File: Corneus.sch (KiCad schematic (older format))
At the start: 146 parts, among them J1 USB_B_Micro, Q1 Q_NPN_BCE, SW1 SW_Push, U1 ATmega32U4-AU, Y1 16MHz

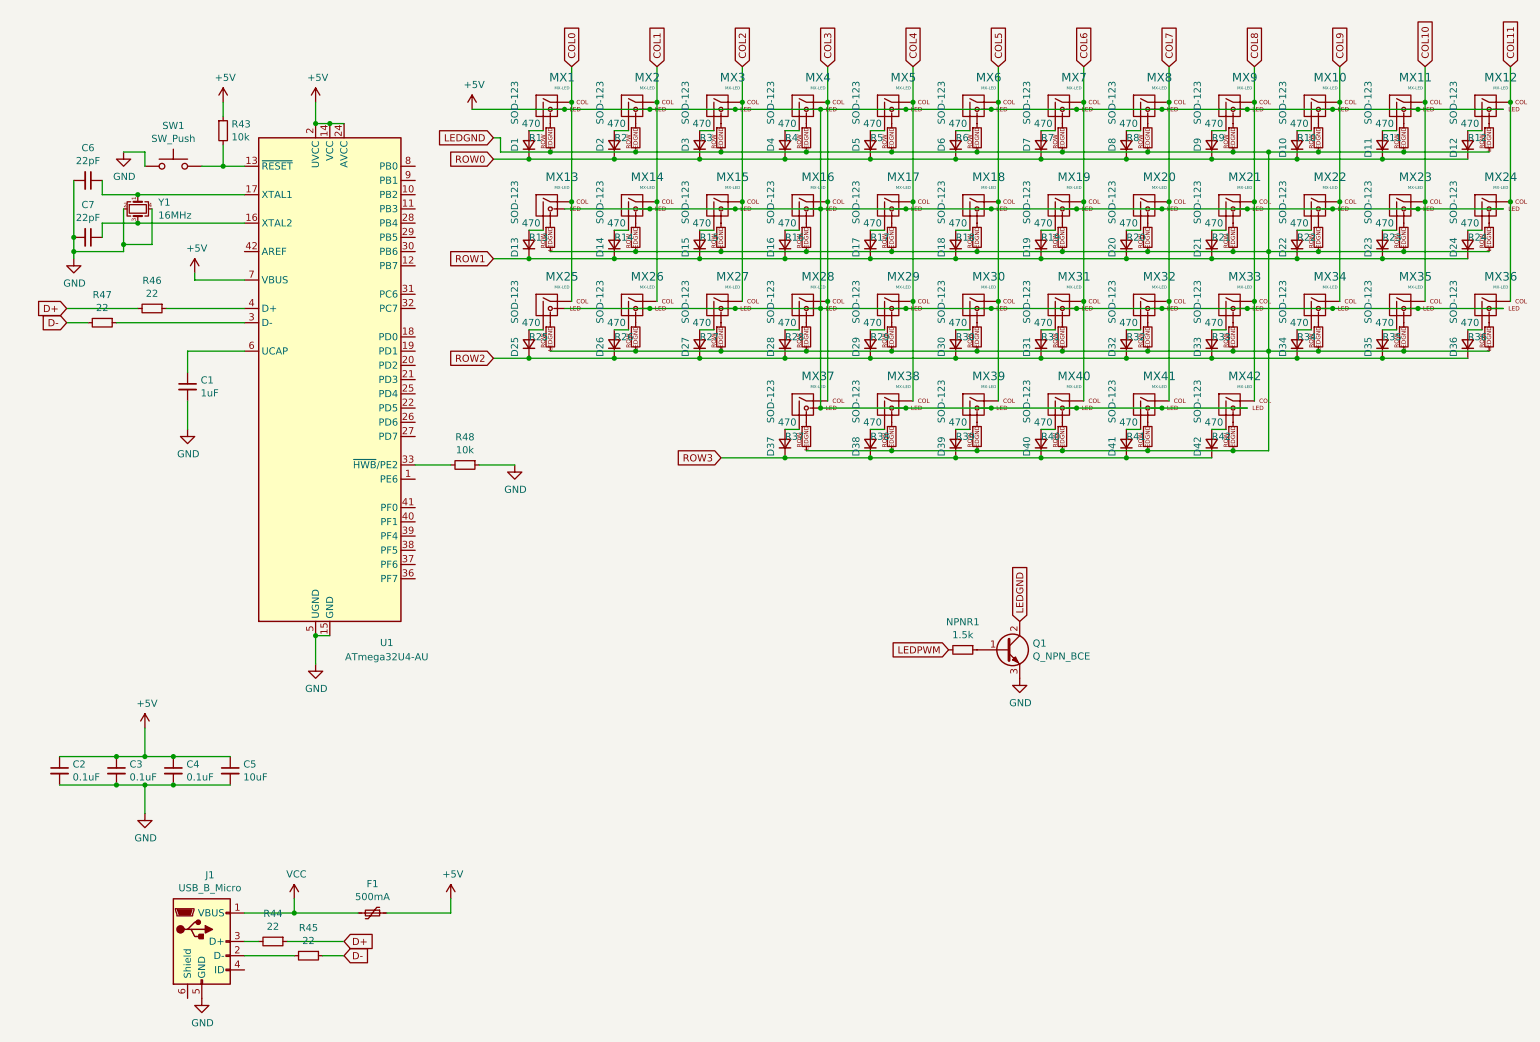
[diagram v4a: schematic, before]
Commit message: added ESD
added ESD IC used in Masterzen's PCB design guide, the CPM43, and the Voyager40
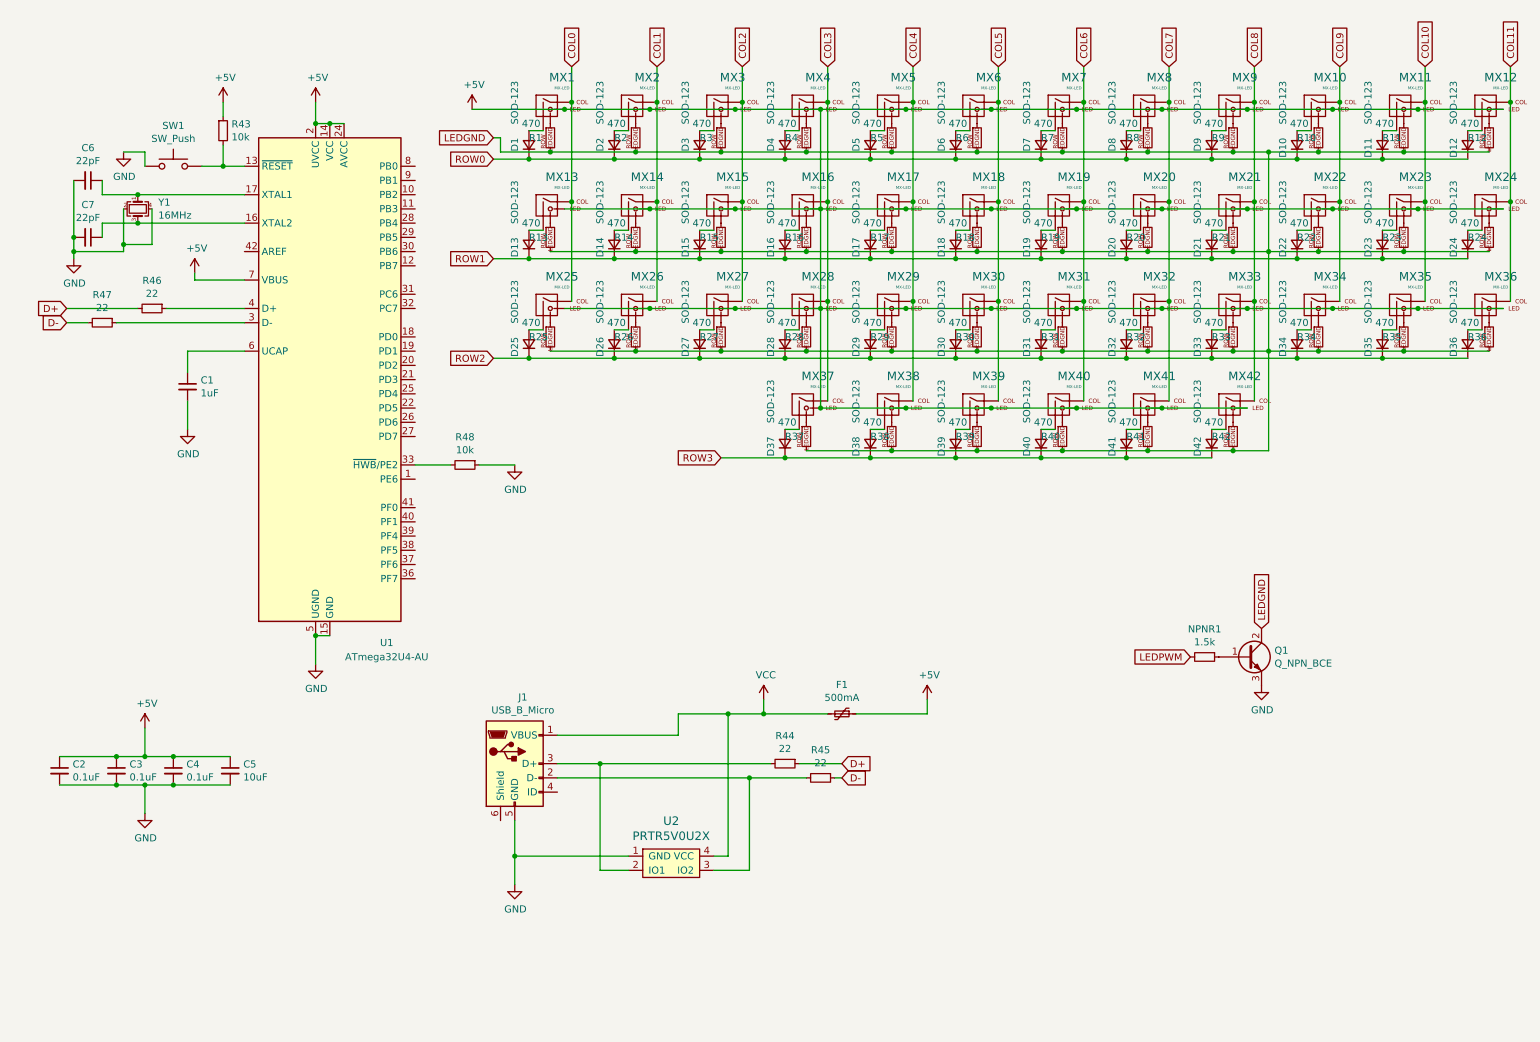
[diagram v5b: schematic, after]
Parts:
- added U2: PRTR5V0U2X, symbol random-keyboard-parts:PRTR5V0U2X
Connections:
- net GND: now also U2.1 (GND)
- net VCC: now also U2.4 (VCC)
- net at J1.2 (D-), R45.2: now also U2.3 (IO2)
- net at J1.3 (D+), R44.2: now also U2.2 (IO1)
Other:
- moved on the sheet: F1, J1, NPNR1, Q1, R44, R45
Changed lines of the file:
@@
 L Connector:USB_B_Micro J1
 U 1 1 5EED7A0C
-P 1800 6950
-F 0 "J1" H 1857 7417 50  0000 C CNN
-F 1 "USB_B_Micro" H 1857 7326 50  0000 C CNN
-F 2 "" H 1950 6900 50  0001 C CNN
-F 3 "~" H 1950 6900 50  0001 C CNN
-	1    1800 6950
+P 4000 5700
+F 0 "J1" H 4057 6167 50  0000 C CNN
+F 1 "USB_B_Micro" H 4057 6076 50  0000 C CNN
+F 2 "" H 4150 5650 50  0001 C CNN
+F 3 "~" H 4150 5650 50  0001 C CNN
+	1    4000 5700
 	1    0    0    -1
 $EndComp
@@
 L Device:Polyfuse_Small F1
 U 1 1 5EED8839
-P 3000 6750
-F 0 "F1" V 2795 6750 50  0000 C CNN
-F 1 "500mA" V 2886 6750 50  0000 C CNN
-F 2 "" H 3050 6550 50  0001 L CNN
-F 3 "~" H 3000 6750 50  0001 C CNN
-	1    3000 6750
+P 6300 5350
+F 0 "F1" V 6095 5350 50  0000 C CNN
+F 1 "500mA" V 6186 5350 50  0000 C CNN
+F 2 "" H 6350 5150 50  0001 L CNN
+F 3 "~" H 6300 5350 50  0001 C CNN
+	1    6300 5350
 	0    1    1    0
 $EndComp
@@
 L power:VCC #PWR?
 U 1 1 5EEDA4E1
-P 2450 6650
-F 0 "#PWR?" H 2450 6500 50  0001 C CNN
-F 1 "VCC" H 2465 6823 50  0000 C CNN
-F 2 "" H 2450 6650 50  0001 C CNN
-F 3 "" H 2450 6650 50  0001 C CNN
-	1    2450 6650
+P 5750 5250
+F 0 "#PWR?" H 5750 5100 50  0001 C CNN
+F 1 "VCC" H 5765 5423 50  0000 C CNN
+F 2 "" H 5750 5250 50  0001 C CNN
+F 3 "" H 5750 5250 50  0001 C CNN
+	1    5750 5250
 	1    0    0    -1
 $EndComp
@@
 L power:+5V #PWR?
 U 1 1 5EEDB21B
-P 3550 6650
-F 0 "#PWR?" H 3550 6500 50  0001 C CNN
-F 1 "+5V" H 3565 6823 50  0000 C CNN
-F 2 "" H 3550 6650 50  0001 C CNN
-F 3 "" H 3550 6650 50  0001 C CNN
-	1    3550 6650
-	1    0    0    -1
-$EndComp
-Wire Wire Line
-	3550 6650 3550 6750
-Wire Wire Line
-	3550 6750 3100 6750
-Wire Wire Line
-	2900 6750 2450 6750
-Wire Wire Line
-	2450 6650 2450 6750
-Connection ~ 2450 6750
-Wire Wire Line
-	2450 6750 2100 6750
-Text GLabel 2800 6950 2    50   Input ~ 0
+P 6900 5250
+F 0 "#PWR?" H 6900 5100 50  0001 C CNN
+F 1 "+5V" H 6915 5423 50  0000 C CNN
+F 2 "" H 6900 5250 50  0001 C CNN
+F 3 "" H 6900 5250 50  0001 C CNN
+	1    6900 5250
+	1    0    0    -1
+$EndComp
+Wire Wire Line
+	6200 5350 5750 5350
+Wire Wire Line
+	5750 5250 5750 5350
+Text GLabel 6300 5700 2    50   Input ~ 0
 D+
-Text GLabel 2800 7050 2    50   Input ~ 0
+Text GLabel 6300 5800 2    50   Input ~ 0
 D-
 $Comp
 L power:GND #PWR?
 U 1 1 5EEDF093
-P 1800 7350
-F 0 "#PWR?" H 1800 7100 50  0001 C CNN
-F 1 "GND" H 1805 7177 50  0000 C CNN
-F 2 "" H 1800 7350 50  0001 C CNN
-F 3 "" H 1800 7350 50  0001 C CNN
-	1    1800 7350
+P 4000 6550
+F 0 "#PWR?" H 4000 6300 50  0001 C CNN
+F 1 "GND" H 4005 6377 50  0000 C CNN
+F 2 "" H 4000 6550 50  0001 C CNN
+F 3 "" H 4000 6550 50  0001 C CNN
+	1    4000 6550
 	1    0    0    -1
 $EndComp
@@
 L Device:Q_NPN_BCE Q1
 U 1 1 5F5CD88C
-P 7450 4900
-F 0 "Q1" H 7641 4946 50  0000 L CNN
-F 1 "Q_NPN_BCE" H 7641 4855 50  0000 L CNN
-F 2 "" H 7650 5000 50  0001 C CNN
-F 3 "~" H 7450 4900 50  0001 C CNN
-	1    7450 4900
+P 9150 4950
+F 0 "Q1" H 9341 4996 50  0000 L CNN
+F 1 "Q_NPN_BCE" H 9341 4905 50  0000 L CNN
+F 2 "" H 9350 5050 50  0001 C CNN
+F 3 "~" H 9150 4950 50  0001 C CNN
+	1    9150 4950
 	1    0    0    -1
 $EndComp
@@
 L Device:R_Small NPNR1
 U 1 1 5F5CF76A
-P 7150 4900
-F 0 "NPNR1" V 6954 4900 50  0000 C CNN
-F 1 "1.5k" V 7045 4900 50  0000 C CNN
-F 2 "" H 7150 4900 50  0001 C CNN
-F 3 "~" H 7150 4900 50  0001 C CNN
-	1    7150 4900
+P 8850 4950
+F 0 "NPNR1" V 8654 4950 50  0000 C CNN
+F 1 "1.5k" V 8745 4950 50  0000 C CNN
+F 2 "" H 8850 4950 50  0001 C CNN
+F 3 "~" H 8850 4950 50  0001 C CNN
+	1    8850 4950
 	0    1    1    0
 $EndComp
-Text GLabel 7050 4900 0    50   Input ~ 0
+Text GLabel 8750 4950 0    50   Input ~ 0
 LEDPWM
 $Comp
 L power:GND #PWR?
 U 1 1 5F5D128A
-P 7550 5100
-F 0 "#PWR?" H 7550 4850 50  0001 C CNN
-F 1 "GND" H 7555 4927 50  0000 C CNN
-F 2 "" H 7550 5100 50  0001 C CNN
-F 3 "" H 7550 5100 50  0001 C CNN
-	1    7550 5100
-	1    0    0    -1
-$EndComp
-Text GLabel 7550 4700 1    50   Input ~ 0
+P 9250 5150
+F 0 "#PWR?" H 9250 4900 50  0001 C CNN
+F 1 "GND" H 9255 4977 50  0000 C CNN
+F 2 "" H 9250 5150 50  0001 C CNN
+F 3 "" H 9250 5150 50  0001 C CNN
+	1    9250 5150
+	1    0    0    -1
+$EndComp
+Text GLabel 9250 4750 1    50   Input ~ 0
 LEDGND
 $Comp
 L Device:R_Small R44
 U 1 1 5F5EB1F7
-P 2300 6950
-F 0 "R44" V 2104 6950 50  0000 C CNN
-F 1 "22" V 2195 6950 50  0000 C CNN
-F 2 "" H 2300 6950 50  0001 C CNN
-F 3 "~" H 2300 6950 50  0001 C CNN
-	1    2300 6950
+P 5900 5700
+F 0 "R44" V 5704 5700 50  0000 C CNN
+F 1 "22" V 5795 5700 50  0000 C CNN
+F 2 "" H 5900 5700 50  0001 C CNN
+F 3 "~" H 5900 5700 50  0001 C CNN
+	1    5900 5700
 	0    1    1    0
 $EndComp
@@
 L Device:R_Small R45
 U 1 1 5F601D9F
-P 2550 7050
-F 0 "R45" V 2354 7050 50  0000 C CNN
-F 1 "22" V 2445 7050 50  0000 C CNN
-F 2 "" H 2550 7050 50  0001 C CNN
-F 3 "~" H 2550 7050 50  0001 C CNN
-	1    2550 7050
+P 6150 5800
+F 0 "R45" V 5954 5800 50  0000 C CNN
+F 1 "22" V 6045 5800 50  0000 C CNN
+F 2 "" H 6150 5800 50  0001 C CNN
+F 3 "~" H 6150 5800 50  0001 C CNN
+	1    6150 5800
 	0    1    1    0
 $EndComp
 Wire Wire Line
-	2100 6950 2200 6950
-Wire Wire Line
-	2400 6950 2800 6950
-Wire Wire Line
-	2100 7050 2450 7050
-Wire Wire Line
-	2650 7050 2800 7050
+	6000 5700 6300 5700
+Wire Wire Line
+	6250 5800 6300 5800
+Wire Wire Line
+	6900 5350 6900 5250
+Wire Wire Line
+	6400 5350 6900 5350
+Wire Wire Line
+	5750 5350 5500 5350
+Wire Wire Line
+	5150 5350 5150 5500
+Connection ~ 5750 5350
+Wire Wire Line
+	4300 5500 5150 5500
+Wire Wire Line
+	4300 5700 4600 5700
+Wire Wire Line
+	4300 5800 5650 5800
+$Comp
+L random-keyboard-parts:PRTR5V0U2X U2
+U 1 1 5F5EB805
+P 5100 6400
+F 0 "U2" H 5100 6697 60  0000 C CNN
+F 1 "PRTR5V0U2X" H 5100 6591 60  0000 C CNN
+F 2 "" H 5100 6400 60  0001 C CNN
+F 3 "" H 5100 6400 60  0001 C CNN
+	1    5100 6400
+	1    0    0    -1
+$EndComp
+Wire Wire Line
+	4800 6450 4600 6450
+Wire Wire Line
+	4600 6450 4600 5700
+Connection ~ 4600 5700
+Wire Wire Line
+	4600 5700 5800 5700
+Wire Wire Line
+	4000 6100 4000 6350
+Wire Wire Line
+	4800 6350 4000 6350
+Connection ~ 4000 6350
+Wire Wire Line
+	4000 6350 4000 6550
+Wire Wire Line
+	5400 6350 5500 6350
+Wire Wire Line
+	5500 6350 5500 5350
+Connection ~ 5500 5350
+Wire Wire Line
+	5500 5350 5150 5350
+Wire Wire Line
+	5400 6450 5650 6450
+Wire Wire Line
+	5650 6450 5650 5800
+Connection ~ 5650 5800
+Wire Wire Line
+	5650 5800 6050 5800
 $EndSCHEMATC

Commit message: remove redundant USB resistors, add submodule for JLCPCB design rules
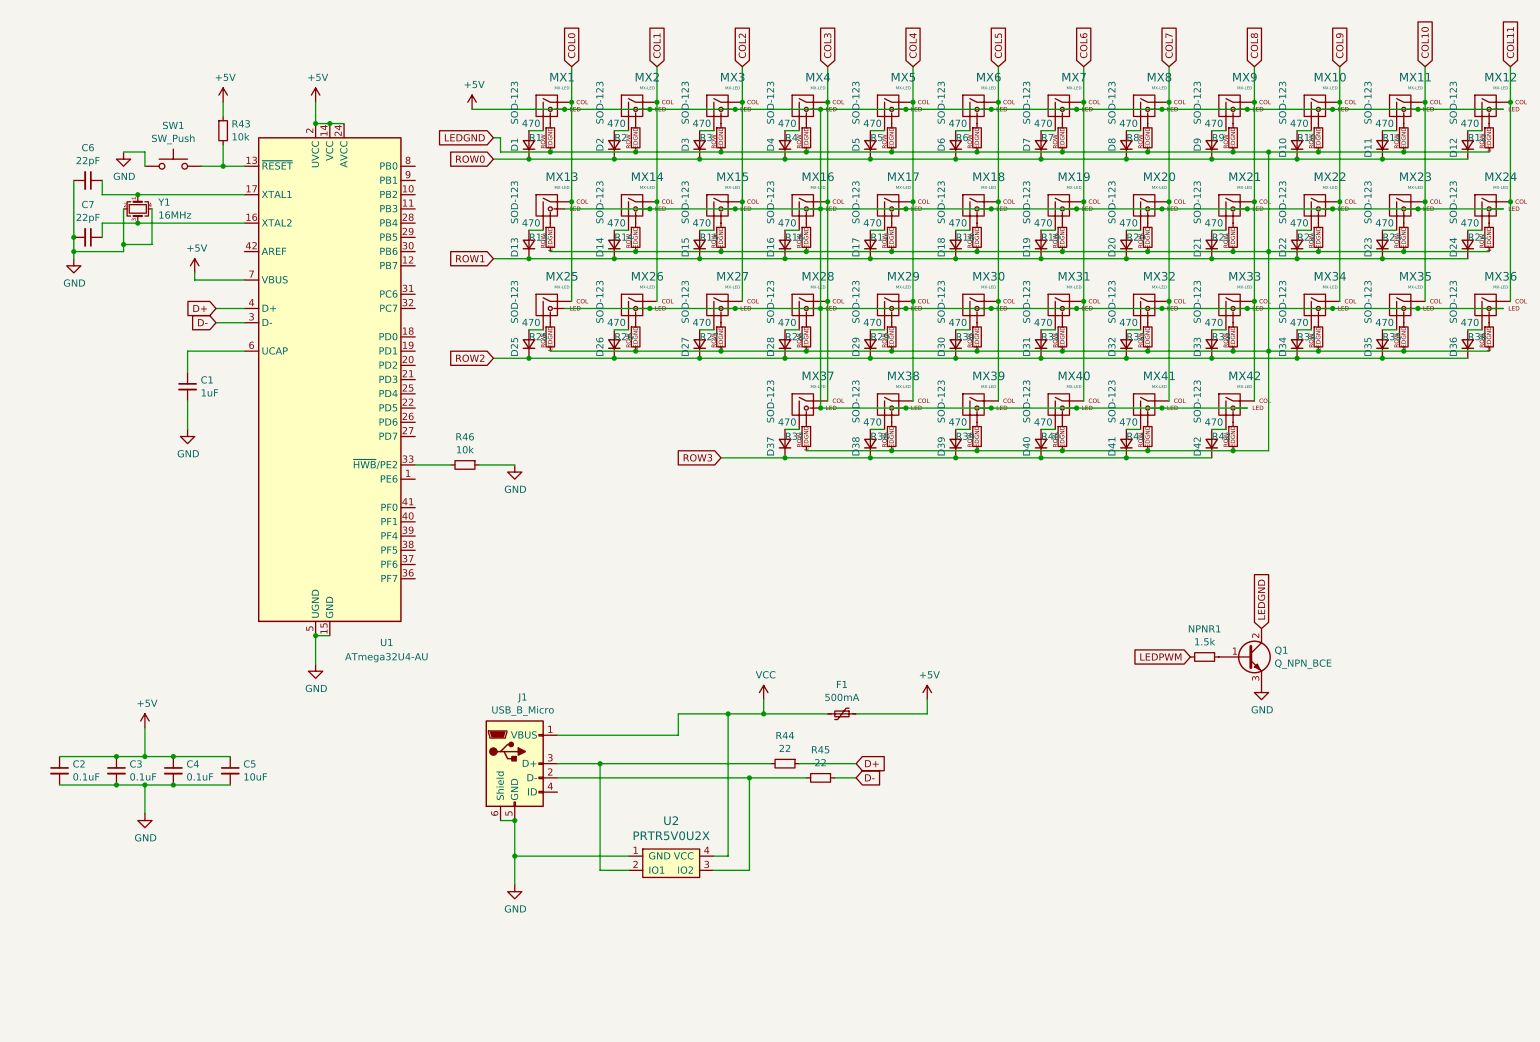
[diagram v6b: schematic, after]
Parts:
- removed R46, R47: 22, symbol Device:R_Small
- C1, C2, C3, C4, C5, C6, C7: footprint (none) -> Capacitor_SMD:C_0805_2012Metric
- D1, D10, D11, D12, D13, D14, D15, D16, D17, D18, D19, D2, D20, D21, D22, D23, D24, D25, D26, D27, D28, D29, D3, D30, D31, D32, D33, D34, D35, D36, D37, D38, D39, D4, D40, D41, D42, D5, D6, D7, D8, D9: footprint (none) -> Diode_SMD:D_SOD-123
- F1: footprint (none) -> Fuse:Fuse_1206_3216Metric
- J1: footprint (none) -> Choco617_parts:CUI_UJ2-MIBH2-4-SMT
- MX1, MX10, MX11, MX12, MX13, MX14, MX15, MX16, MX17, MX18, MX19, MX2, MX20, MX21, MX22, MX23, MX24, MX25, MX26, MX27, MX28, MX29, MX3, MX30, MX31, MX32, MX33, MX34, MX35, MX36, MX37, MX38, MX39, MX4, MX40, MX41, MX42, MX5, MX6, MX7, MX8, MX9: footprint (none) -> Choco617_parts:Kailh_socket_MX_PCBmount_LED_1U
- NPNR1, R1, R10, R11, R12, R13, R14, R15, R16, R17, R18, R19, R2, R20, R21, R22, R23, R24, R25, R26, R27, R28, R29, R3, R30, R31, R32, R33, R34, R35, R36, R37, R38, R39, R4, R40, R41, R42, R43, R44, R45, R5, R6, R7, R8, R9: footprint (none) -> Resistor_SMD:R_0805_2012Metric
- Q1: footprint (none) -> Package_TO_SOT_SMD:SOT-223
- R46: renamed from R48; footprint (none) -> Resistor_SMD:R_0805_2012Metric
- SW1: footprint (none) -> random-keyboard-parts:SKQG-1155865
- U2: footprint (none) -> random-keyboard-parts:SOT143B
- Y1: footprint (none) -> Crystal:Crystal_SMD_3225-4Pin_3.2x2.5mm
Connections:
- net D+: now also U1.4 (D+)
- net D-: now also U1.3 (D-)
- net GND: now also J1.6 (Shield)
